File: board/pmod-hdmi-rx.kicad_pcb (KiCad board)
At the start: 2 copper layers, 37.3 x 43.2 mm, 35 parts, among them P1 PMOD-CONN_6X2, U31 XC9140, U32 REG710-DBV

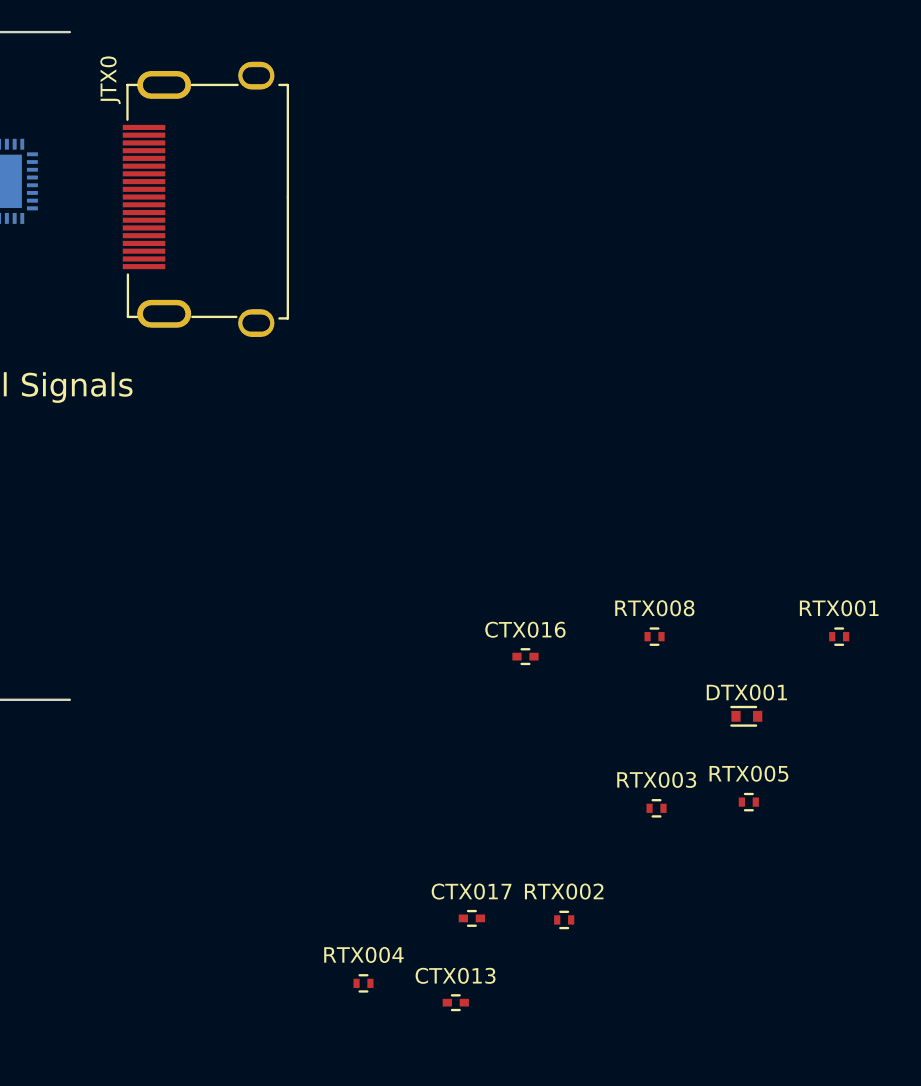
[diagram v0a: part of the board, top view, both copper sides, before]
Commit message: s/tx/rx/
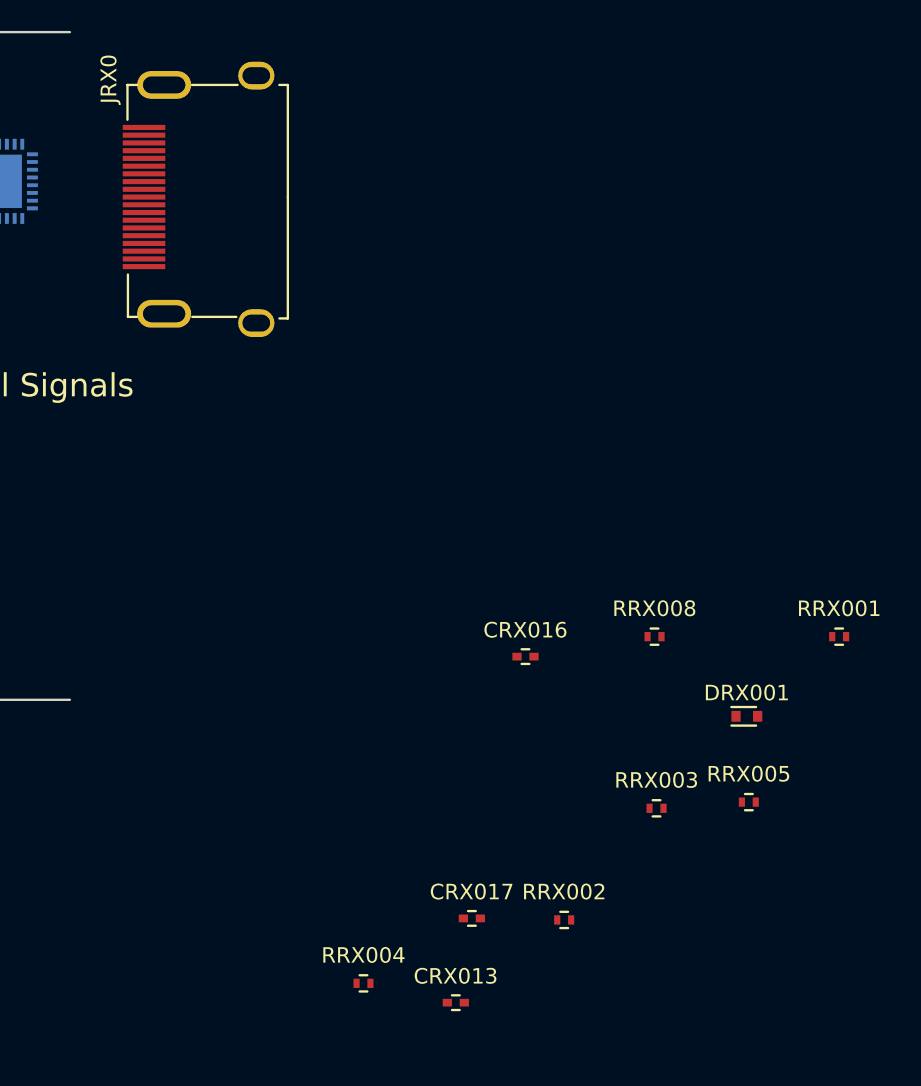
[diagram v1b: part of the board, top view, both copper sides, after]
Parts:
- renumbered CTX001 to CRX001, CTX002 to CRX002, CTX003 to CRX003, CTX004 to CRX004, CTX005 to CRX005, CTX006 to CRX006, CTX007 to CRX007, CTX008 to CRX008, CTX013 to CRX013, CTX016 to CRX016, CTX017 to CRX017, DTX001 to DRX001, JTX0 to JRX0, RTX001 to RRX001, RTX002 to RRX002, RTX003 to RRX003, RTX004 to RRX004, RTX005 to RRX005, RTX008 to RRX008, UTX0 to URX0
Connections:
- net /HDMI TX/HDMIP_TX0_CLK+ renamed /HDMI RX/HDMIP_RX0_CLK+
- net /HDMI TX/HDMIP_TX0_CLK- renamed /HDMI RX/HDMIP_RX0_CLK-
- net /HDMI TX/HDMIP_TX0_D0+ renamed /HDMI RX/HDMIP_RX0_D0+
- net /HDMI TX/HDMIP_TX0_D0- renamed /HDMI RX/HDMIP_RX0_D0-
- net /HDMI TX/HDMIP_TX0_D1+ renamed /HDMI RX/HDMIP_RX0_D1+
- net /HDMI TX/HDMIP_TX0_D1- renamed /HDMI RX/HDMIP_RX0_D1-
- net /HDMI TX/HDMIP_TX0_D2+ renamed /HDMI RX/HDMIP_RX0_D2+
- net /HDMI TX/HDMIP_TX0_D2- renamed /HDMI RX/HDMIP_RX0_D2-
- net /HDMI TX/HDMIP_TX0_HPD renamed /HDMI RX/HDMIP_RX0_HPD
- net /HDMI TX/HDMIP_TX0_SCL renamed /HDMI RX/HDMIP_RX0_SCL
- net /HDMI TX/HDMIP_TX0_SDA renamed /HDMI RX/HDMIP_RX0_SDA
- net /HDMI_TX0_CEC renamed /HDMI_RX0_CEC
- net /HDMI_TX0_CLK+ renamed /HDMI_RX0_CLK+
- net /HDMI_TX0_CLK- renamed /HDMI_RX0_CLK-
- net /HDMI_TX0_D0+ renamed /HDMI_RX0_D0+
- net /HDMI_TX0_D0- renamed /HDMI_RX0_D0-
- net /HDMI_TX0_D1+ renamed /HDMI_RX0_D1+
- net /HDMI_TX0_D1- renamed /HDMI_RX0_D1-
- net /HDMI_TX0_D2+ renamed /HDMI_RX0_D2+
- net /HDMI_TX0_D2- renamed /HDMI_RX0_D2-
- net /HDMI_TX0_DCC_EN renamed /HDMI_RX0_DCC_EN
- net /HDMI_TX0_DDET renamed /HDMI_RX0_DDET
- net /HDMI_TX0_EQ0 renamed /HDMI_RX0_EQ0
- net /HDMI_TX0_EQ1 renamed /HDMI_RX0_EQ1
- net /HDMI_TX0_HPD renamed /HDMI_RX0_HPD
- net /HDMI_TX0_SCL renamed /HDMI_RX0_SCL
- net /HDMI_TX0_SDA renamed /HDMI_RX0_SDA
- net /~HDMI_TX0_OE renamed /~HDMI_RX0_OE
- net TX05V0 renamed RX05V0

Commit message: Updating the PCB.
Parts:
- removed CRX016, CRX017: 0.1uF, Capacitors_SMD:C_0402
- removed RDC1, RDE1, REQ0, REQ1, ROE1: 10k, Resistors_SMD:R_0402
- added CRX009: 10nF, Capacitors_SMD:C_0402, F.Cu at (102.4, 93.1)
- added CRX010: 0.1uF, Capacitors_SMD:C_0402, F.Cu at (95.4, 99.2)
- added CRX011: 10nF, Capacitors_SMD:C_0402, F.Cu at (76.0, 105.9)
- added CRX012: 10nF, Capacitors_SMD:C_0402, F.Cu at (88.4, 105.3)
- added CRX014: 10nF, Capacitors_SMD:C_0402, F.Cu at (82.1, 111.6)
- added CRX015: 10uF, Capacitors_SMD:C_0603, F.Cu at (75.9, 118.2)
- added D0: LED, LEDs:LED_0603, F.Cu at (101.0, 143.6)
- added D1: LED, LEDs:LED_0603, F.Cu at (105.3, 138.2)
- added DRX002: D, Diodes_SMD:SOD-123, F.Cu at (75.9, 112.1)
- added DRX003: D, Diodes_SMD:SOD-123, F.Cu at (90.0, 93.4)
- added FBRX001: FILTER, Capacitors_SMD:C_0805, F.Cu at (69.3, 106.0)
- added FBRX002: FILTER, Capacitors_SMD:C_0805, F.Cu at (76.4, 93.5)
- added FBRX003: FILTER, Capacitors_SMD:C_0805, F.Cu at (69.3, 99.7)
- added FBRX004: FILTER, Capacitors_SMD:C_0805, F.Cu at (69.3, 93.5)
- added PE1: CONN_02X02, Pin_Headers:Pin_Header_Straight_2x02, F.Cu at (84.4, 130.3)
- added PWP1: CONN_02X01, Pin_Headers:Pin_Header_Straight_1x02, F.Cu at (70.8, 137.2)
- added QRX001: FDV301N, TO_SOT_Packages_SMD:SOT-23, F.Cu at (76.4, 99.9)
- added QRX002: FDV301N, TO_SOT_Packages_SMD:SOT-23, F.Cu at (83.4, 93.6)
- added QRX003: FDV301N, TO_SOT_Packages_SMD:SOT-23, F.Cu at (69.3, 112.4)
- added RD0: 100, Resistors_SMD:R_0402, F.Cu at (87.8, 143.4)
- added RD1: 100, Resistors_SMD:R_0402, F.Cu at (92.3, 134.0)
- added RPE1: 10k, Resistors_SMD:R_0402, F.Cu at (92.8, 139.8)
- added RRX006: 100K, Resistors_SMD:R_0402, F.Cu at (107.8, 98.8)
- added RRX007: 100K, Resistors_SMD:R_0402, F.Cu at (101.6, 104.5)
- added RRX009: 47K, Resistors_SMD:R_0402, F.Cu at (94.6, 110.4)
- added RRX010: 1K, Resistors_SMD:R_0402, F.Cu at (88.3, 116.5)
- added RRX011: 47K, Resistors_SMD:R_0402, F.Cu at (108.6, 93.2)
- added RRX012: 1K, Resistors_SMD:R_0402, F.Cu at (101.6, 98.8)
- added RTX1: 10k, Resistors_SMD:R_0402, F.Cu at (102.4, 132.8)
- added RWP1: 10k, Resistors_SMD:R_0402, F.Cu at (97.1, 139.8)
- added UE1: 24AA01/24LC01B, TO_SOT_Packages_SMD:SOT-23-5, F.Cu at (72.6, 127.7)
- CRX001, CRX002, CRX003: value 0.1uF -> 10uF; footprint Capacitors_SMD:C_0402 -> Capacitors_SMD:C_0603; moved to F.Cu
- CRX004, CRX005, CRX006, CRX007: moved to F.Cu
- CRX008: value 0.1uF -> 10nF; moved to F.Cu
- CRX013: value 10n -> 0.1nF
- CV5: footprint Capacitors_SMD:C_1206 -> Capacitors_SMD:C_0603
- DRX001: value D -> LED; footprint Diodes_SMD:SOD-523 -> LEDs:LED_0603
- JRX0: value HDMI_OUT -> HDMI_IN
- RRX001, RRX002: value 2k2 -> 100K
- RRX003: value 12k4 -> 1K
- RRX004: value 2k2 -> 560R
- RRX005: value 2k2 -> 2K
- RRX008: value 27K -> 100K
- URX0: value PTN3363 -> AD8195; footprint Housings_DFN_QFN:QFN-32-1EP_5x5mm_Pitch0.5mm -> Housings_DFN_QFN:QFN-40-1EP_6x6mm_Pitch0.5mm; moved to F.Cu
- moved CRX007 80.7 mm to (58.9, 106.7)
- moved CRX008 80.7 mm to (53.3, 106.7)
- moved CRX005 73.2 mm to (58.9, 102.9)
- moved CRX006 73.2 mm to (53.3, 102.9)
- moved CRX003 66.8 mm to (58.9, 99.6)
- moved CRX004 66.8 mm to (53.3, 99.6)
- moved CRX001 60.9 mm to (58.9, 96.5)
- moved CRX002 60.9 mm to (53.3, 96.5)
- moved DRX001 60.9 mm to (68.9, 118.2)
- moved R31 54.0 mm to (70.9, 144.5)
- moved RRX001 50.8 mm to (82.2, 106.0)
- moved R32 49.0 mm to (67.4, 144.5)
- moved RRX005 47.9 mm to (82.1, 117.1)
- moved RRX008 47.2 mm to (88.4, 110.9)
- moved U32 40.1 mm to (81.0, 138.7)
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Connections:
- CRX001 pad 1: Net-(CRX001-Pad1) -> /HDMI RX/AVCC3V3
- CRX001 pad 2: /HDMI_RX0_CLK+ -> GND
- CRX002 pad 1: Net-(CRX002-Pad1) -> /HDMI RX/VTTO3V3
- CRX002 pad 2: /HDMI_RX0_CLK- -> GND
- CRX003 pad 1: Net-(CRX003-Pad1) -> /HDMI RX/VTTI3V3
- CRX003 pad 2: /HDMI_RX0_D0+ -> GND
- CRX004 pad 1: Net-(CRX004-Pad1) -> /HDMI RX/AVCC3V3
- CRX004 pad 2: /HDMI_RX0_D0- -> GND
- CRX005 pad 1: Net-(CRX005-Pad1) -> /HDMI RX/VTTO3V3
- CRX005 pad 2: /HDMI_RX0_D1+ -> GND
- CRX006 pad 1: Net-(CRX006-Pad1) -> /HDMI RX/VTTI3V3
- CRX006 pad 2: /HDMI_RX0_D1- -> GND
- CRX007 pad 1: Net-(CRX007-Pad1) -> /HDMI RX/AVCC3V3
- CRX007 pad 2: /HDMI_RX0_D2+ -> GND
- CRX008 pad 1: Net-(CRX008-Pad1) -> /HDMI RX/VTTO3V3
- CRX008 pad 2: /HDMI_RX0_D2- -> GND
- CRX013 pad 1: GND -> Net-(CRX013-Pad1)
- CRX013 pad 2: /HDMI RX/HDMIP_RX0_HPD -> GND
- CV5 pad 1: RX05V0 -> VCC5V0
- DRX001 pad 1: /HDMI_RX0_CEC -> Net-(DRX001-Pad1)
- DRX001 pad 2: Net-(DRX001-Pad2) -> /HDMI RX/VCC5V0_RX0
- JRX0 pad 11: GND -> Net-(JRX0-Pad11)
- JRX0 pad 13: /HDMI_RX0_CEC -> /HDMI RX/HDMIP_RX0_CEC
- JRX0 pad 18: RX05V0 -> Net-(FBRX004-Pad1)
- P1 pad 10: /HDMI_RX0_DCC_EN -> /HDMI_RX0_TXEN
- P1 pad 2: /HDMI_RX0_HPD -> /HDMI RX/HDMI_RX0_HPA
- P1 pad 3: /HDMI_RX0_EQ1 -> /HDMI_RX0_IO1
- P1 pad 4: /HDMI_RX0_DDET -> /HDMI_RX0_PEEN
- P1 pad 9: /HDMI_RX0_EQ0 -> /HDMI_RX0_IO0
- R32 pad 1: Net-(R32-Pad1) -> /HDMI_RX0_IO0
- RRX001 pad 1: VCC3V3 -> GND
- RRX001 pad 2: /HDMI_RX0_SDA -> /HDMI RX/HDMI_RX0_HPD
- RRX002 pad 1: VCC3V3 -> Net-(QRX001-Pad3)
- RRX002 pad 2: /HDMI_RX0_SCL -> /HDMI RX/VCC5V0_RX0
- RRX003 pad 1: Net-(RRX003-Pad1) -> /HDMI RX/HDMIP_RX0_HPD
- RRX003 pad 2: GND -> /HDMI RX/VCC5V0_RX0
- RRX004 pad 1: RX05V0 -> Net-(QRX003-Pad3)
- RRX004 pad 2: /HDMI RX/HDMIP_RX0_SCL -> Net-(DRX001-Pad1)
- RRX005 pad 1: RX05V0 -> /HDMI RX/HDMIP_RX0_CLK-
- RRX005 pad 2: /HDMI RX/HDMIP_RX0_SDA -> Net-(JRX0-Pad11)
- RRX008 pad 1: VCC3V3 -> /HDMI_RX0_TXEN
- RRX008 pad 2: Net-(DRX001-Pad2) -> GND
- U31 pad 4: RX05V0 -> VCC5V0
- U32 pad 1: RX05V0 -> VCC5V0
- U32 pad 3: Net-(R32-Pad1) -> /HDMI_RX0_IO0
- URX0 pad 1: VCC3V3 -> /HDMI RX/HDMIP_RX0_CLK-
- URX0 pad 10: /HDMI RX/HDMIP_RX0_D2- -> /HDMI RX/AVCC3V3
- URX0 pad 11: /HDMI RX/HDMIP_RX0_D1+ -> /HDMI_RX0_CLK-
- URX0 pad 12: /HDMI RX/HDMIP_RX0_D1- -> /HDMI_RX0_CLK+
- URX0 pad 13: /HDMI RX/HDMIP_RX0_D0+ -> /HDMI RX/VTTO3V3
- URX0 pad 14: /HDMI RX/HDMIP_RX0_D0- -> /HDMI_RX0_D0-
- URX0 pad 15: /HDMI RX/HDMIP_RX0_CLK+ -> /HDMI_RX0_D0+
- URX0 pad 16: /HDMI RX/HDMIP_RX0_CLK- -> /HDMI RX/AVCC3V3
- URX0 pad 17: /~HDMI_RX0_OE -> /HDMI_RX0_D1-
- URX0 pad 18: VCC3V3 -> /HDMI_RX0_D1+
- URX0 pad 19: /HDMI RX/HDMIP_RX0_SCL -> /HDMI_RX0_D2-
- URX0 pad 2: /HDMI_RX0_EQ1 -> /HDMI RX/HDMIP_RX0_CLK+
- URX0 pad 20: /HDMI RX/HDMIP_RX0_SDA -> /HDMI_RX0_D2+
- URX0 pad 21: /HDMI RX/HDMIP_RX0_HPD -> Net-(CRX015-Pad1)
- URX0 pad 22: /HDMI_RX0_DCC_EN -> /HDMI RX/AVCC3V3
- URX0 pad 23: (no net) -> /HDMI RX/AVCC3V3
- URX0 pad 25: Net-(CRX002-Pad1) -> /HDMI RX/AVCC3V3
- URX0 pad 26: Net-(CRX001-Pad1) -> /HDMI RX/AVCC3V3
- URX0 pad 27: Net-(CRX004-Pad1) -> GND
- URX0 pad 28: Net-(CRX003-Pad1) -> /HDMI_RX0_TXEN
- URX0 pad 29: Net-(CRX006-Pad1) -> /HDMI_RX0_PEEN
- URX0 pad 3: /HDMI_RX0_DDET -> /HDMI RX/HDMIP_RX0_D0-
- URX0 pad 30: Net-(CRX005-Pad1) -> /HDMI RX/AVCC3V3
- URX0 pad 31: Net-(CRX008-Pad1) -> /HDMI_RX0_CEC
- URX0 pad 32: Net-(CRX007-Pad1) -> Net-(CRX013-Pad1)
- URX0 pad 33: GND -> VCC3V3
- URX0 pad 4: Net-(RRX003-Pad1) -> /HDMI RX/HDMIP_RX0_D0+
- URX0 pad 5: /HDMI_RX0_HPD -> /HDMI RX/VTTI3V3
- URX0 pad 6: /HDMI_RX0_SDA -> /HDMI RX/HDMIP_RX0_D1-
- URX0 pad 7: /HDMI_RX0_SCL -> /HDMI RX/HDMIP_RX0_D1+
- URX0 pad 8: /HDMI_RX0_EQ0 -> /HDMI RX/HDMIP_RX0_D2-
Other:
- board size 37.3 x 43.2 mm -> 61.2 x 43.2 mm

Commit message: First version from Phyllis.
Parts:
- CRX001, CRX002, CRX003, CRX004, CRX005, CRX006, CRX007, CRX008, CRX009, CRX010, CRX011, CRX012, CRX013, CRX014, FBRX001, FBRX002, FBRX003, RPE1, RRX010, RRX012, RTX1, RWP1: moved to B.Cu
- moved P1 70.2 mm to (85.3, 80.2)
- moved JRX0 64.9 mm to (114.3, 83.2)
- moved URX0 62.7 mm to (101.4, 81.6)
- moved CRX008 61.9 mm to (106.7, 75.3), turned to 0 degrees
- moved CRX006 57.7 mm to (106.7, 80.9), turned to 0 degrees
- moved CRX002 56.5 mm to (106.7, 78.0), turned to 0 degrees
- moved CRX005 54.5 mm to (106.7, 76.6), turned to 0 degrees
- moved DRX001 53.9 mm to (116.8, 93.7), turned to 180 degrees
- moved QRX003 52.7 mm to (119.4, 96.0)
- moved CRX003 51.8 mm to (106.7, 79.5), turned to 0 degrees
- moved PWP1 50.9 mm to (102.4, 97.3), turned to 270 degrees
- moved R31 47.7 mm to (91.7, 101.6), turned to 270 degrees
- moved CRX007 47.6 mm to (99.0, 81.0), turned to 0 degrees
- moved CRX004 47.4 mm to (98.0, 83.8)
- moved CRX001 47.1 mm to (104.4, 84.1), turned to 90 degrees
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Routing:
- net VCC3V3: track 0.00 -> 124.8 mm, vias 0 -> 3
- net GND: track 0.00 -> 57.4 mm, vias 0 -> 27
- net /HDMI_RX0_D2+: track 0.00 -> 53.3 mm
- net /HDMI_RX0_D2-: track 0.00 -> 49.5 mm
- net /HDMI_RX0_D1+: track 0.00 -> 48.9 mm
- net /HDMI_RX0_D0+: track 0.00 -> 47.4 mm
- net /HDMI_RX0_D1-: track 0.00 -> 44.8 mm
- net /HDMI_RX0_D0-: track 0.00 -> 42.0 mm
- net /HDMI RX/AVCC3V3: track 0.00 -> 31.8 mm, vias 0 -> 5
- net /HDMI_RX0_TXEN: track 0.00 -> 31.8 mm
- net /HDMI_RX0_PEEN: track 0.00 -> 28.9 mm
- net /HDMI_RX0_SDA: track 0.00 -> 27.8 mm
- net /HDMI_RX0_SCL: track 0.00 -> 27.0 mm
- net /HDMI_RX0_IO0: track 0.00 -> 26.1 mm
- net /HDMI_RX0_CEC: track 0.00 -> 25.0 mm, vias 0 -> 1
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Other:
- board size 61.2 x 43.2 mm -> 42 x 43.3 mm
- net class Default: trace_width 0.25 -> 0.127; via_dia 0.6 -> 0.5; via_drill 0.4 -> 0.25
- net class PWR added: clearance 0.2, trace_width 0.25, via_dia 0.5, via_drill 0.25
- rule trace_min: 0.2 -> 0.127
- rule via_min_drill: 0.3 -> 0.25
- rule via_min_size: 0.4 -> 0.5
- board text added: "101.24"
- board text added: "104.34"
- board text added: "113.182"
- board text added: "122.24"
- board text added: "13.5"
- board text added: "15.0"
- board text added: "2.842"
- board text added: "21.0"
- board text added: "31.496"
- board text added: "42.0"
- board text added: "43.18"
- board text added: "70.002"
- board text added: "72.844"
- board text added: "75.84"
- board text added: "80.24"
- board text added: "90.84"

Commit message: Second version from Phyllis.
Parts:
- CRX007, CRX010, RPE1, RRX010, RRX012, RTX1: moved to F.Cu
- RRX005, RRX009: moved to B.Cu
- moved D0 24.0 mm to (83.9, 90.3), turned to 90 degrees
- moved RTX1 22.5 mm to (91.3, 83.9)
- moved RPE1 21.7 mm to (94.6, 83.9)
- moved RD0 19.9 mm to (83.9, 92.8), turned to 270 degrees
- moved D1 14.3 mm to (86.6, 90.3)
- moved RD1 13.9 mm to (86.6, 92.8), turned to 270 degrees
- moved RRX010 9.76 mm to (94.0, 88.0), turned to 90 degrees
- moved RRX012 9.42 mm to (95.4, 88.0), turned to 90 degrees
- moved CRX007 8.41 mm to (94.5, 73.9), turned to 90 degrees
- moved FBRX003 7.97 mm to (110.2, 76.5), turned to 90 degrees
- moved CRX010 5.92 mm to (95.6, 74.9), turned to 90 degrees
- moved RRX009 5.83 mm to (113.9, 86.1), turned to 270 degrees
- moved CRX001 5.47 mm to (107.2, 88.8), turned to 270 degrees
- moved CRX009 5.46 mm to (108.7, 77.1), turned to 90 degrees
- moved CRX002 5.25 mm to (105.9, 72.8), turned to 90 degrees
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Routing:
- net GND: track 57.4 -> 359.2 mm, vias 27 -> 116
- net /HDMI_RX0_D2+: track 53.3 -> 22.9 mm, vias 0 -> 1
- net /HDMI_RX0_D1+: track 48.9 -> 22.8 mm, vias 0 -> 1
- net /HDMI_RX0_D0+: track 47.4 -> 21.4 mm, vias 0 -> 1
- net /HDMI_RX0_D2-: track 49.5 -> 24.0 mm, vias 0 -> 1
- net /HDMI_RX0_D1-: track 44.8 -> 23.8 mm, vias 0 -> 1
- net /HDMI RX/AVCC3V3: track 31.8 -> 50.8 mm, vias 5 -> 3
- net /HDMI_RX0_D0-: track 42.0 -> 24.0 mm, vias 0 -> 1
- net VCC5V0: track 4.60 -> 20.8 mm, vias 0 -> 3
- net /HDMI_RX0_IO0: track 26.1 -> 35.9 mm
- net VCC3V3: track 124.8 -> 133.1 mm, vias 3 -> 7
- net /HDMI RX/VTTI3V3: track 6.28 -> 12.4 mm
- net /HDMI RX/HDMIP_RX0_CLK-: track 9.34 -> 14.0 mm, vias 0 -> 1
- net /HDMI_RX0_CEC: track 25.0 -> 20.9 mm
- net /HDMI_RX0_CLK+: track 21.1 -> 24.0 mm, vias 0 -> 1
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- added copper zone on B.Cu, net GND
- added copper zone on F.Cu, net GND
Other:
- board text added: "1 OZ CU ALL LAYERS, WHEN FINISHED."
- board text added: "1. MATERIAL: FR408 1.6 mm THK, 4 LAYERS, EQUALLY SPACED,"
- board text added: "2. PLATED HOLES TO HAVE 1/2 OZ CU MIN."
- board text added: "3. PURPLE SOLDERMASK OVER BARE CU, BOTH SIDES"
- board text added: "4. ENIG (ELECTROLESS NICKEL IMMERSION GOLD)"
- board text added: "5. PERMANENTLY MARK DATE CODE AND"
- board text added: "CEC"
- board text added: "CLK+"
- board text added: "CLK-"
- board text added: "D0+"
- board text added: "D0-"
- board text added: "D1+"
- board text added: "D1-"
- board text added: "D2-"
- board text added: "EN"
- board text added: "GND"
- board text added: "HPA"
- board text added: "High Speed"
- board text added: "IO0"
- board text added: "IO1"
- board text added: "Low Speed & Control Signals"
- board text added: "MANUFACTURING SYMBOL ON BOTTOM."
- board text added: "NOTES: (UNLESS OTHERWISE SPECIFIED)"
- board text added: "PEEN"
- board text added: "SDA"
- board text added: "TEMPORARY LAYER - SHOWS GRIDS USED TO OBTAIN DIMENSIONS"
- board text added: "TOP"
- board text added: "TX"
- board text added: "TXEN"
- board text added: "VCC"
- board text removed: "/\ High Speed Signals"
- board text removed: "\/ Low Speed & Control Signals"
